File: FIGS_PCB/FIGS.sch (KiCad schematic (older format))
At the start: 66 parts

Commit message: PCB for FIGS
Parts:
- removed Q? (x5): Q_NMOS_DGS, symbol Device:Q_NMOS_DGS
- added Q1, Q2, Q3, Q4, Q5: FDV303N, FDV303N:SOT96P237X111-3N, symbol FDV303N:FDV303N
- BT1: renamed from BT?; footprint (none) -> Connector_PinHeader_2.54mm:PinHeader_1x02_P2.54mm_Vertical
- C1, C10, C2, C3, C5, C6, C7, C8, C9: renamed from C?; footprint (none) -> Capacitor_SMD:C_0805_2012Metric_Pad1.18x1.45mm_HandSolder
- C11, C4: renamed from C?; footprint (none) -> Capacitor_Tantalum_SMD:CP_EIA-7260-28_AVX-M_Pad2.68x6.30mm_HandSolder
- D1, D2, D3, D4, D5, D6: renamed from D?; footprint (none) -> LED_THT:LED_D3.0mm
- D7: renamed from D?; footprint (none) -> Diode_SMD:D_MicroMELF_Handsoldering
- IC1: renamed from IC?; footprint QFP80P1200X1200X160-44N -> CY8C4245AXI-483:QFP80P1200X1200X160-44N
- J1: renamed from J?; footprint (none) -> Connector_PinHeader_1.27mm:PinHeader_1x08_P1.27mm_Horizontal
- J10: renamed from J?; footprint (none) -> Connector_PinHeader_1.27mm:PinHeader_1x02_P1.27mm_Horizontal
- J2: renamed from J?; footprint (none) -> Connector_PinHeader_1.27mm:PinHeader_2x04_P1.27mm_Vertical
- J3, J4: renamed from J?; footprint (none) -> Connector_PinHeader_1.27mm:PinHeader_1x04_P1.27mm_Horizontal
- J5, J6, J7, J9: renamed from J?; footprint (none) -> Connector_PinHeader_1.27mm:PinHeader_1x03_P1.27mm_Horizontal
- J8: renamed from J?; footprint (none) -> Connector_PinHeader_1.27mm:PinHeader_2x05_P1.27mm_Horizontal
- R1, R10, R11, R12, R13, R14, R15, R16, R17, R18, R19, R2, R20, R21, R22, R23, R24, R25, R26, R27, R28, R3, R4, R5, R6, R7, R8, R9: renamed from R?; footprint (none) -> Resistor_SMD:R_1206_3216Metric_Pad1.30x1.75mm_HandSolder
- SW1: renamed from SW?; footprint (none) -> Button_Switch_THT:SW_CuK_JS202011CQN_DPDT_Straight
- SW2: renamed from SW?; footprint (none) -> Button_Switch_THT:SW_PUSH_6mm_H4.3mm
- U1: renamed from U?; footprint (none) -> TLV1117-33CDCY:SOT230P700X180-4N
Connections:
- wire segments 279 -> 292
- no-connect marks 1 -> 8
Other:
- note added: "Power Flags to avoid \n software error"
- moved on the sheet: D7, J10, R16, R17, R18, R19, R22, R23, R25, R28

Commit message: PCB changed
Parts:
- removed R1, R3, R5, R7: 5.6k, Resistor_SMD:R_1206_3216Metric_Pad1.30x1.75mm_HandSolder, symbol Device:R
- removed R10, R9: 0, Resistor_SMD:R_1206_3216Metric_Pad1.30x1.75mm_HandSolder, symbol Device:R
- removed R2, R4, R6, R8: nc, Resistor_SMD:R_1206_3216Metric_Pad1.30x1.75mm_HandSolder, symbol Device:R
- added H1, H2, H3, H4: MountingHole, MountingHole:MountingHole_2.7mm, symbol Mechanical:MountingHole
- added TP1, TP2: TestPoint, TestPoint:TestPoint_Pad_D3.0mm, symbol Connector:TestPoint
- C11, C4: footprint Capacitor_Tantalum_SMD:CP_EIA-7260-28_AVX-M_Pad2.68x6.30mm_HandSolder -> Capacitor_Tantalum_SMD:CP_EIA-7132-20_AVX-U_Pad2.72x3.50mm_HandSolder
- J1: footprint Connector_PinHeader_1.27mm:PinHeader_1x08_P1.27mm_Horizontal -> Connector_PinHeader_2.54mm:PinHeader_1x08_P2.54mm_Horizontal
- J10: footprint Connector_PinHeader_1.27mm:PinHeader_1x02_P1.27mm_Horizontal -> Connector_PinHeader_2.54mm:PinHeader_1x02_P2.54mm_Horizontal
- J2: footprint Connector_PinHeader_1.27mm:PinHeader_2x04_P1.27mm_Vertical -> Connector_PinHeader_2.54mm:PinHeader_2x04_P2.54mm_Horizontal
- J3, J4: footprint Connector_PinHeader_1.27mm:PinHeader_1x04_P1.27mm_Horizontal -> Connector_PinHeader_2.54mm:PinHeader_1x04_P2.54mm_Horizontal
- J5, J6, J7, J9: footprint Connector_PinHeader_1.27mm:PinHeader_1x03_P1.27mm_Horizontal -> Connector_PinHeader_2.54mm:PinHeader_1x03_P2.54mm_Horizontal
- J8: footprint Connector_PinHeader_1.27mm:PinHeader_2x05_P1.27mm_Horizontal -> Connector_PinHeader_2.54mm:PinHeader_2x05_P2.54mm_Vertical
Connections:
- net +3V3: now also J3.4 (Pin_4), J8.2 (Pin_2); no longer J3.1 (Pin_1), J8.1 (Pin_1)
- net +BATT: now also J5.2 (Pin_2), J6.2 (Pin_2), J7.2 (Pin_2), J9.2 (Pin_2); no longer J5.1 (Pin_1), J6.1 (Pin_1), J7.1 (Pin_1), J9.1 (Pin_1)
- net BT_UART_RX: now also IC1.25 ((GPIO)_P0[1]), J3.1 (Pin_1), R12.1; no longer J3.3 (Pin_3)
- net BT_UART_TX: now also IC1.24 ((GPIO)_P0[0]), R13.2
- net CTRLS0: now also J5.1 (Pin_1); no longer J5.2 (Pin_2)
- net CTRLS1: now also J6.1 (Pin_1); no longer J6.2 (Pin_2)
- net CTRLS2: now also J7.1 (Pin_1); no longer J7.2 (Pin_2)
- net CTRLS3: now also J9.1 (Pin_1); no longer J9.2 (Pin_2)
- net GNDA: now also J3.3 (Pin_3), J8.1 (Pin_1); no longer J3.4 (Pin_4), J8.2 (Pin_2)
- net IMU_SCL: now also J4.3 (Pin_3), R11.2; no longer J4.2 (Pin_2), R14.2
- net IMU_SDA: now also J4.2 (Pin_2), R14.2; no longer J4.3 (Pin_3), R11.2
- net KP_RX: now also J8.9 (Pin_9), R12.2; no longer J8.8 (Pin_8), R13.1
- net KP_TX: now also J8.7 (Pin_7), R13.1; no longer J8.10 (Pin_10), R12.2
- net SWD_CLK: now also J8.6 (Pin_6); no longer J8.5 (Pin_5)
- net SWD_IO: now also J8.4 (Pin_4); no longer J8.3 (Pin_3)
- net TUNER_SCL: now also J8.8 (Pin_8); no longer J8.7 (Pin_7)
- net TUNER_SDA: now also J8.10 (Pin_10); no longer J8.9 (Pin_9)
- net VIBRATION: now also TP1.1, TP2.1
- net XRES: now also J8.3 (Pin_3); no longer J8.4 (Pin_4)
- removed net Rx_1: IC1.24 ((GPIO)_P0[0]), R12.1
- removed net Tx_1: IC1.25 ((GPIO)_P0[1]), R13.2
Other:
- moved on the sheet: J2, J6, J7, J9

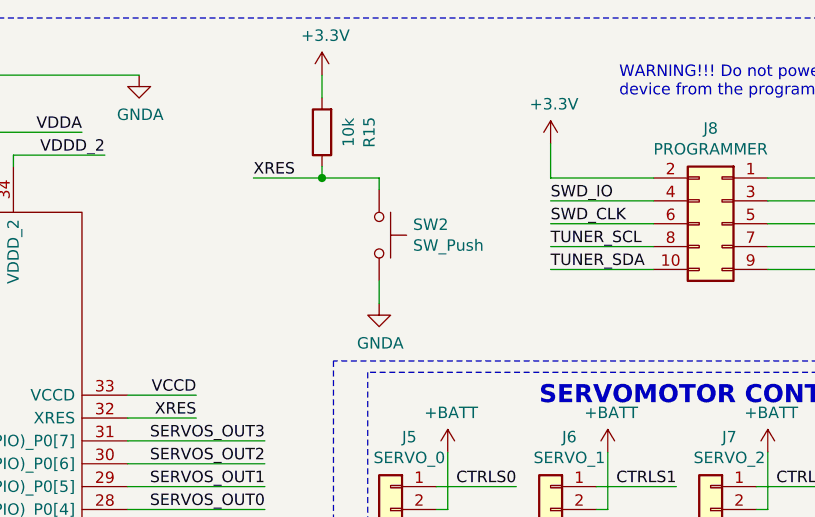
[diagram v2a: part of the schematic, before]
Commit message: added Pullups on tuner SCL/SDA lines
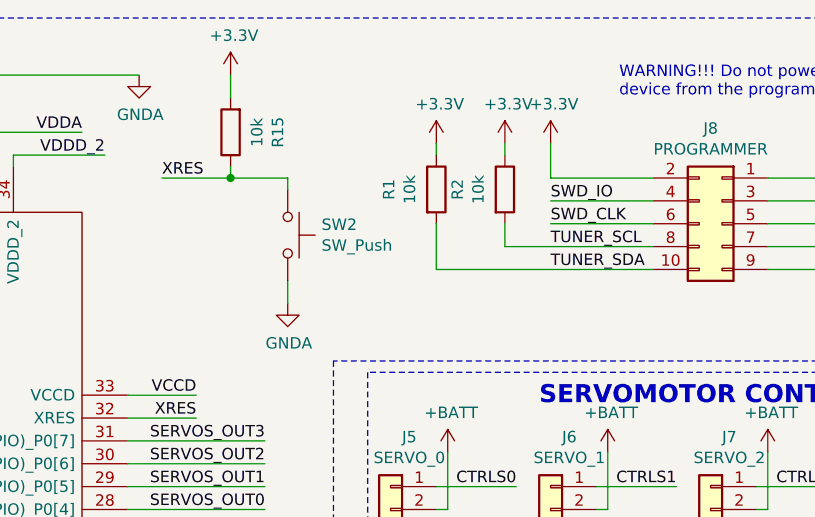
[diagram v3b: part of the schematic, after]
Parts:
- added R1, R2: 10k, Resistor_SMD:R_1206_3216Metric_Pad1.30x1.75mm_HandSolder, symbol Device:R
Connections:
- net +3V3: now also R1.1, R2.1
- net TUNER_SCL: now also R2.2
- net TUNER_SDA: now also R1.2
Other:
- moved on the sheet: R15, SW2
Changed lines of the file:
@@
 L Device:R R15
 U 1 1 603DE7D5
-P 6550 1000
-F 0 "R15" V 6343 1000 50  0000 C CNN
-F 1 "10k" V 6434 1000 50  0000 C CNN
-F 2 "Resistor_SMD:R_1206_3216Metric_Pad1.30x1.75mm_HandSolder" V 6480 1000 50  0001 C CNN
-F 3 "~" H 6550 1000 50  0001 C CNN
-	1    6550 1000
+P 6150 1000
+F 0 "R15" V 5943 1000 50  0000 C CNN
+F 1 "10k" V 6034 1000 50  0000 C CNN
+F 2 "Resistor_SMD:R_1206_3216Metric_Pad1.30x1.75mm_HandSolder" V 6080 1000 50  0001 C CNN
+F 3 "~" H 6150 1000 50  0001 C CNN
+	1    6150 1000
 	-1   0    0    1
 $EndComp
@@
 L power:+3.3V #PWR035
 U 1 1 604229A9
-P 6550 750
-F 0 "#PWR035" H 6550 600 50  0001 C CNN
-F 1 "+3.3V" H 6565 923 50  0000 C CNN
-F 2 "" H 6550 750 50  0001 C CNN
-F 3 "" H 6550 750 50  0001 C CNN
-	1    6550 750
-	1    0    0    -1
-$EndComp
-Wire Wire Line
-	6550 750  6550 850
+P 6150 750
+F 0 "#PWR035" H 6150 600 50  0001 C CNN
+F 1 "+3.3V" H 6165 923 50  0000 C CNN
+F 2 "" H 6150 750 50  0001 C CNN
+F 3 "" H 6150 750 50  0001 C CNN
+	1    6150 750
+	1    0    0    -1
+$EndComp
+Wire Wire Line
+	6150 750  6150 850
 $Comp
 L Switch:SW_Push SW2
 U 1 1 6042ADAB
-P 6800 1450
-F 0 "SW2" V 6754 1598 50  0000 L CNN
-F 1 "SW_Push" V 6845 1598 50  0000 L CNN
-F 2 "Button_Switch_THT:SW_PUSH_6mm_H4.3mm" H 6800 1650 50  0001 C CNN
-F 3 "~" H 6800 1650 50  0001 C CNN
-	1    6800 1450
+P 6400 1450
+F 0 "SW2" V 6354 1598 50  0000 L CNN
+F 1 "SW_Push" V 6445 1598 50  0000 L CNN
+F 2 "Button_Switch_THT:SW_PUSH_6mm_H4.3mm" H 6400 1650 50  0001 C CNN
+F 3 "~" H 6400 1650 50  0001 C CNN
+	1    6400 1450
 	0    1    1    0
 $EndComp
 Wire Wire Line
-	6550 1150 6550 1200
-Wire Wire Line
-	6550 1200 6800 1200
-Wire Wire Line
-	6800 1200 6800 1250
+	6150 1150 6150 1200
+Wire Wire Line
+	6150 1200 6400 1200
+Wire Wire Line
+	6400 1200 6400 1250
 $Comp
 L power:GNDA #PWR036
 U 1 1 60434021
-P 6800 1750
-F 0 "#PWR036" H 6800 1500 50  0001 C CNN
-F 1 "GNDA" H 6805 1577 50  0000 C CNN
-F 2 "" H 6800 1750 50  0001 C CNN
-F 3 "" H 6800 1750 50  0001 C CNN
-	1    6800 1750
-	1    0    0    -1
-$EndComp
-Wire Wire Line
-	6800 1650 6800 1750
-Text Label 6250 1200 0    50   ~ 0
+P 6400 1750
+F 0 "#PWR036" H 6400 1500 50  0001 C CNN
+F 1 "GNDA" H 6405 1577 50  0000 C CNN
+F 2 "" H 6400 1750 50  0001 C CNN
+F 3 "" H 6400 1750 50  0001 C CNN
+	1    6400 1750
+	1    0    0    -1
+$EndComp
+Wire Wire Line
+	6400 1650 6400 1750
+Text Label 5850 1200 0    50   ~ 0
 XRES
 Wire Wire Line
-	6250 1200 6550 1200
-Connection ~ 6550 1200
+	5850 1200 6150 1200
+Connection ~ 6150 1200
 Wire Wire Line
 	5700 2150 6000 2150
@@
 Wire Wire Line
 	7550 1300 8000 1300
-Wire Wire Line
-	7550 1500 8000 1500
 Text Label 7550 1400 0    50   ~ 0
 SWD_CLK
@@
 Wire Wire Line
 	7550 1400 8000 1400
-Wire Wire Line
-	7550 1600 8000 1600
 Wire Wire Line
 	8500 1600 8950 1600
@@
 Wire Wire Line
 	5700 3150 6300 3150
+Wire Wire Line
+	7350 1500 8000 1500
+$Comp
+L Device:R R2
+U 1 1 604A00DA
+P 7350 1250
+F 0 "R2" V 7143 1250 50  0000 C CNN
+F 1 "10k" V 7234 1250 50  0000 C CNN
+F 2 "Resistor_SMD:R_1206_3216Metric_Pad1.30x1.75mm_HandSolder" V 7280 1250 50  0001 C CNN
+F 3 "~" H 7350 1250 50  0001 C CNN
+	1    7350 1250
+	1    0    0    -1
+$EndComp
+$Comp
+L Device:R R1
+U 1 1 604A1DCF
+P 7050 1250
+F 0 "R1" V 6843 1250 50  0000 C CNN
+F 1 "10k" V 6934 1250 50  0000 C CNN
+F 2 "Resistor_SMD:R_1206_3216Metric_Pad1.30x1.75mm_HandSolder" V 6980 1250 50  0001 C CNN
+F 3 "~" H 7050 1250 50  0001 C CNN
+	1    7050 1250
+	1    0    0    -1
+$EndComp
+$Comp
+L power:+3.3V #PWR022
+U 1 1 604A2372
+P 7350 1050
+F 0 "#PWR022" H 7350 900 50  0001 C CNN
+F 1 "+3.3V" H 7365 1223 50  0000 C CNN
+F 2 "" H 7350 1050 50  0001 C CNN
+F 3 "" H 7350 1050 50  0001 C CNN
+	1    7350 1050
+	1    0    0    -1
+$EndComp
+$Comp
+L power:+3.3V #PWR021
+U 1 1 604A27A9
+P 7050 1050
+F 0 "#PWR021" H 7050 900 50  0001 C CNN
+F 1 "+3.3V" H 7065 1223 50  0000 C CNN
+F 2 "" H 7050 1050 50  0001 C CNN
+F 3 "" H 7050 1050 50  0001 C CNN
+	1    7050 1050
+	1    0    0    -1
+$EndComp
+Wire Wire Line
+	7050 1050 7050 1100
+Wire Wire Line
+	7350 1050 7350 1100
+Wire Wire Line
+	7350 1400 7350 1500
+Wire Wire Line
+	7050 1400 7050 1600
+Wire Wire Line
+	7050 1600 8000 1600
 $EndSCHEMATC
